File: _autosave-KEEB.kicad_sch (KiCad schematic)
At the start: 20 parts

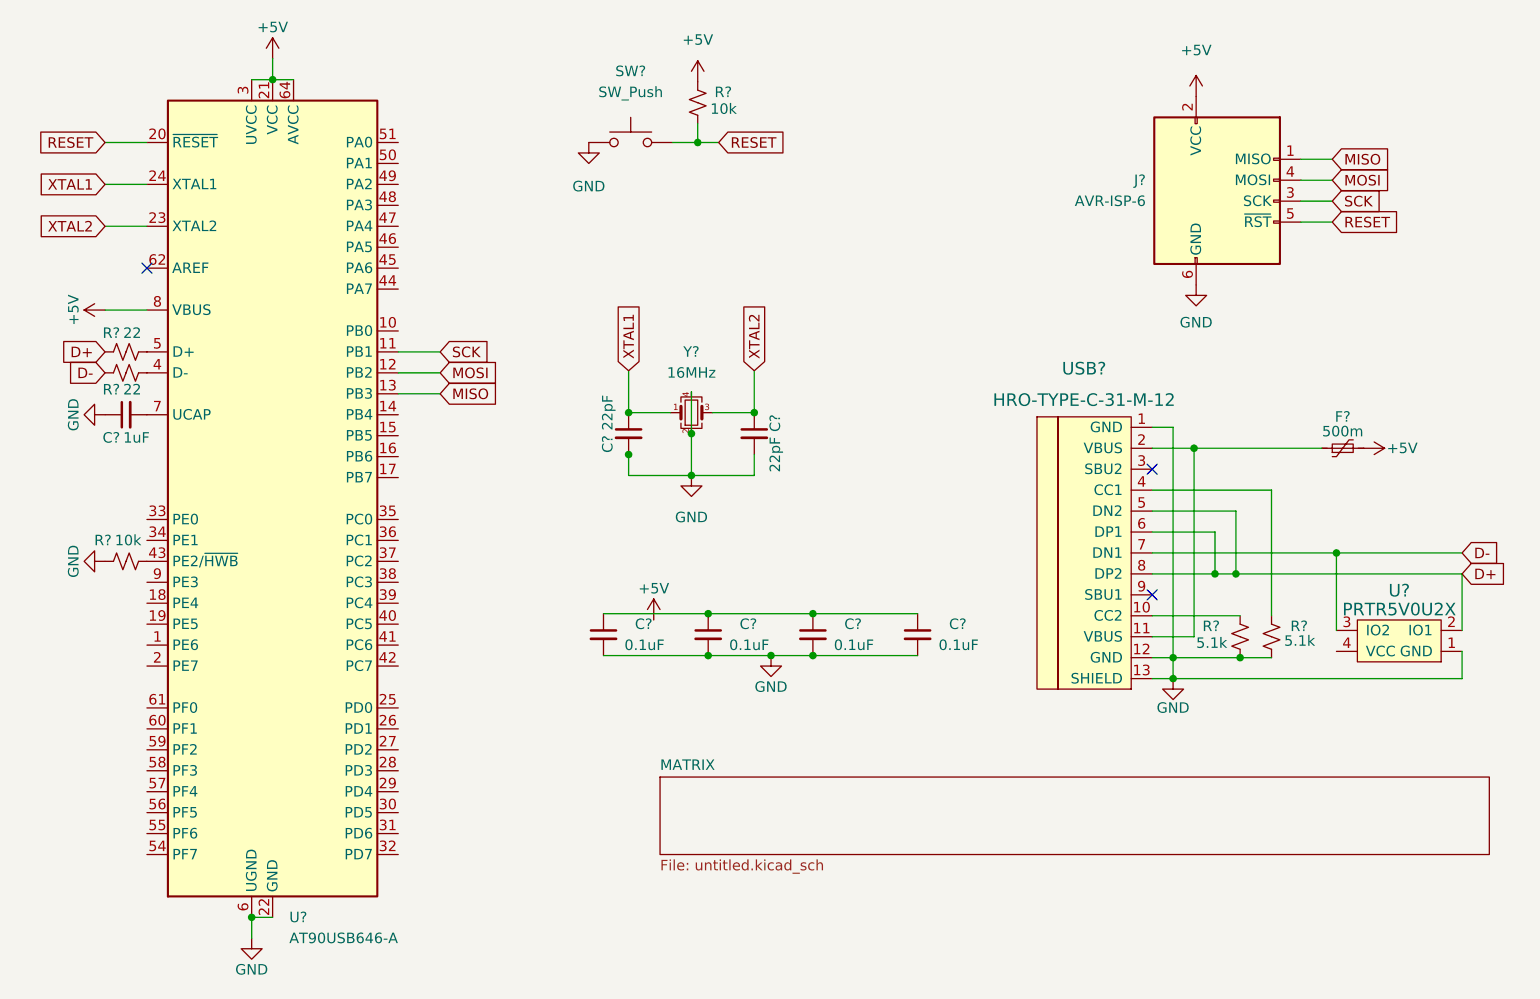
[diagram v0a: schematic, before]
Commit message: Rearranged schematic
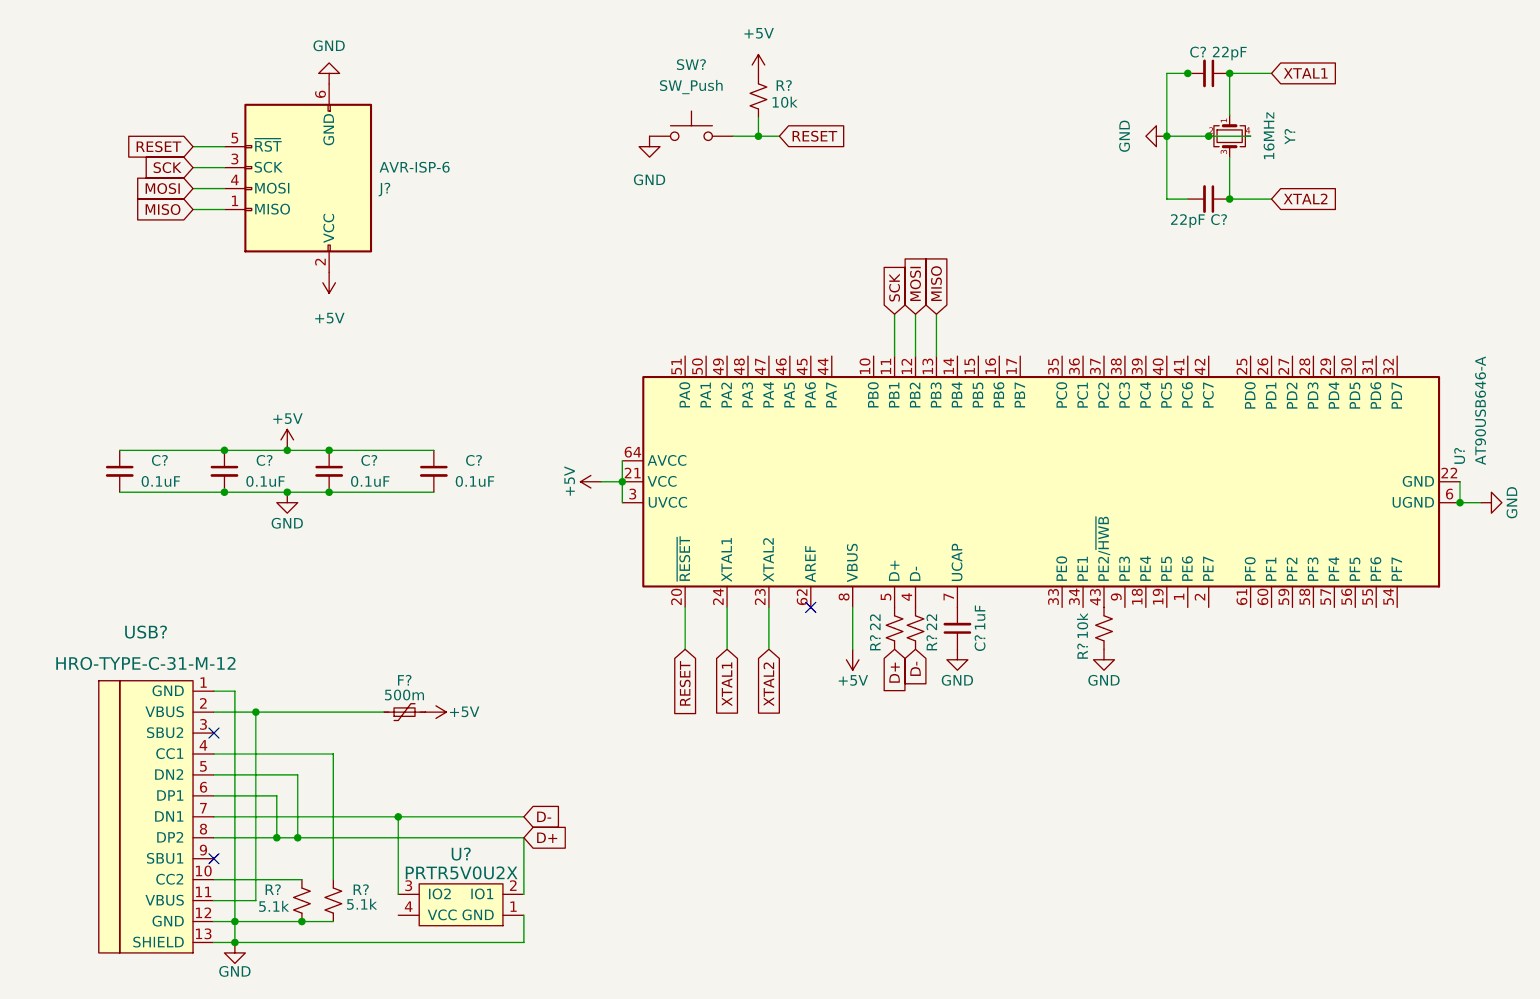
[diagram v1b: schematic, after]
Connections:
- net +5V: now also C?.1, C?.1, C?.1, C?.1
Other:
- removed sheet MATRIX
- moved on the sheet: C?, F?, J?, R?, SW?, U?, USB?, Y?
